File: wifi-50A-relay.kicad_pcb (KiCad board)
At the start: 2 copper layers, 85 x 56 mm, 42 parts, among them J1 PROG, J2 100k_HOT, J3 100k_COLD, K1 J115F21C12VDCS.9, K2 J115F21C12VDCS.9, Q1 AO3400A, SW1 SKRKAEE020, U1 ESP-WROOM-02, U2 TPS54331DR, U3 ADS1115IDGS

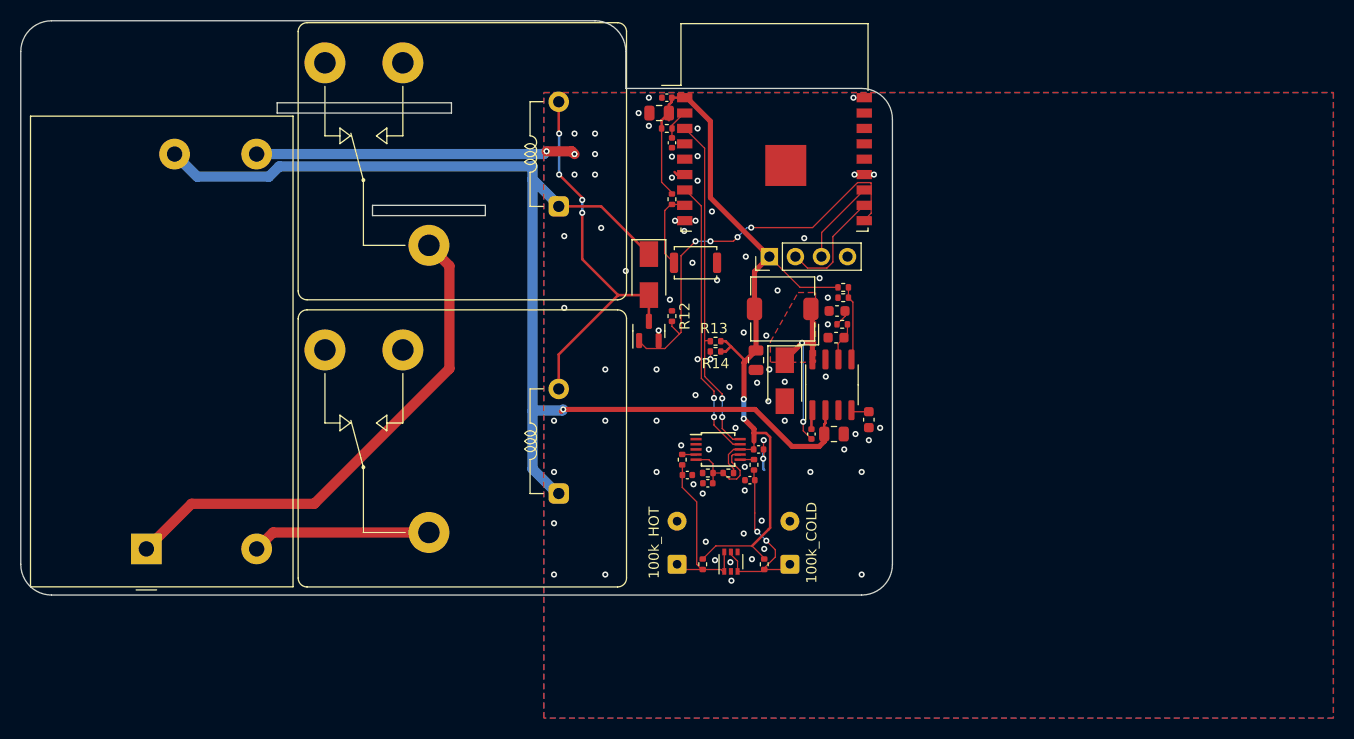
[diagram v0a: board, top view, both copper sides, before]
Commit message: Add kibot & fix DRC issues from kicad update
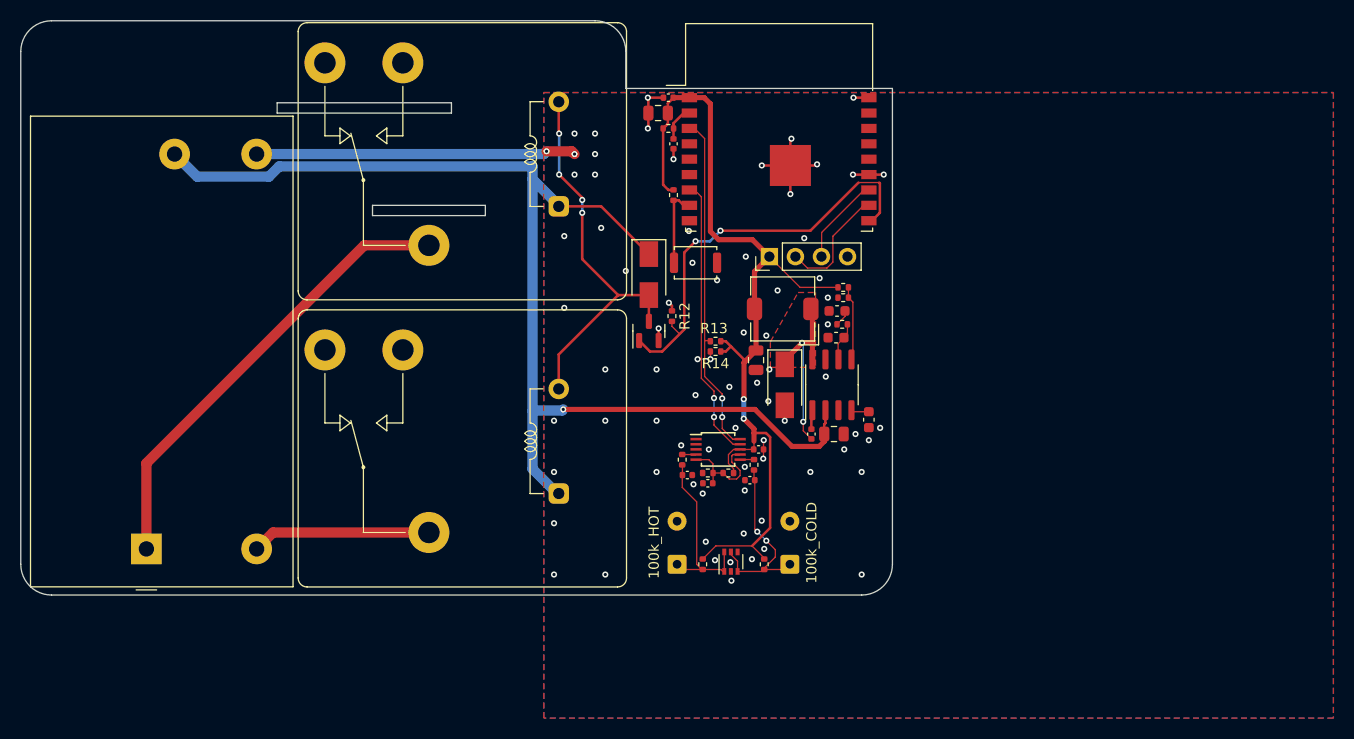
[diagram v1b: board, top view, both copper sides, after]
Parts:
- moved U1 0.45 mm to (102.0, 44.5)
- moved R3 0.43 mm to (91.7, 48.0)
- moved D1 0.40 mm to (102.5, 66.5)
- moved C8 0.18 mm to (91.7, 43.0)
- moved C5 0.15 mm to (91.2, 38.5)
- moved R2 0.15 mm to (91.2, 41.5)
- moved C3 0.10 mm to (90.2, 40.0)
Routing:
- net GND: track 36.0 -> 56.1 mm, vias 80 -> 75
- net /AC_PH_2: track 49.7 -> 44.7 mm
- net /SW: track 39.5 -> 42.9 mm, vias 4 -> 2
- net +3V3: track 88.2 -> 90.3 mm
- net Net-(C12-Pad1): track 18.4 -> 17.1 mm
- net Net-(C11-Pad1): track 17.5 -> 16.7 mm
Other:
- outline, holes or cut-outs redrawn

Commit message: Fix erc issues
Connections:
- net +3V3 renamed +3.3V
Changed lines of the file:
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@@
   (net 2 "+12V")
   (net 3 "Net-(C2-Pad1)")
-  (net 4 "+3V3")
+  (net 4 "+3.3V")
   (net 5 "Net-(C4-Pad1)")
   (net 6 "Net-(C6-Pad1)")
@@
     (fp_line (start 1 0.625) (end -1 0.625) (layer "F.Fab") (width 0.1))
     (pad "1" smd roundrect (at -0.95 0 180) (size 1 1.45) (layers "F.Cu" "F.Paste" "F.Mask") (roundrect_rratio 0.25)
-      (net 4 "+3V3") (pintype "passive"))
+      (net 4 "+3.3V") (pintype "passive"))
     (pad "2" smd roundrect (at 0.95 0 180) (size 1 1.45) (layers "F.Cu" "F.Paste" "F.Mask") (roundrect_rratio 0.25)
       (net 1 "GND") (pintype "passive"))
@@
     (fp_line (start -0.5 -0.25) (end 0.5 -0.25) (layer "F.Fab") (width 0.1))
     (pad "1" smd roundrect (at -0.48 0 180) (size 0.56 0.62) (layers "F.Cu" "F.Paste" "F.Mask") (roundrect_rratio 0.25)
-      (net 4 "+3V3") (pintype "passive"))
+      (net 4 "+3.3V") (pintype "passive"))
     (pad "2" smd roundrect (at 0.48 0 180) (size 0.56 0.62) (layers "F.Cu" "F.Paste" "F.Mask") (roundrect_rratio 0.25)
       (net 1 "GND") (pintype "passive"))
@@
     (fp_line (start -1 -0.625) (end 1 -0.625) (layer "F.Fab") (width 0.1))
     (pad "1" smd roundrect (at -0.95 0 270) (size 1 1.45) (layers "F.Cu" "F.Paste" "F.Mask") (roundrect_rratio 0.25)
-      (net 4 "+3V3") (pintype "passive"))
+      (net 4 "+3.3V") (pintype "passive"))
     (pad "2" smd roundrect (at 0.95 0 270) (size 1 1.45) (layers "F.Cu" "F.Paste" "F.Mask") (roundrect_rratio 0.25)
       (net 1 "GND") (pintype "passive"))
@@
     (fp_line (start -0.5 0.25) (end -0.5 -0.25) (layer "F.Fab") (width 0.1))
     (pad "1" smd roundrect (at -0.48 0) (size 0.56 0.62) (layers "F.Cu" "F.Paste" "F.Mask") (roundrect_rratio 0.25)
-      (net 4 "+3V3") (pintype "passive"))
+      (net 4 "+3.3V") (pintype "passive"))
     (pad "2" smd roundrect (at 0.48 0) (size 0.56 0.62) (layers "F.Cu" "F.Paste" "F.Mask") (roundrect_rratio 0.25)
       (net 1 "GND") (pintype "passive"))
@@
     (fp_line (start -1.27 8.89) (end -1.27 -0.635) (layer "F.Fab") (width 0.1))
     (pad "1" thru_hole rect (at 0 0 90) (size 1.7 1.7) (drill 1) (layers *.Cu *.Mask)
-      (net 4 "+3V3") (pinfunction "Pin_1") (pintype "passive"))
+      (net 4 "+3.3V") (pinfunction "Pin_1") (pintype "passive"))
     (pad "2" thru_hole oval (at 0 2.54 90) (size 1.7 1.7) (drill 1) (layers *.Cu *.Mask)
       (net 16 "Net-(J1-Pad2)") (pinfunction "Pin_2") (pintype "passive"))
@@
       (net 7 "Net-(C7-Pad2)") (pinfunction "1") (pintype "passive"))
     (pad "2" smd roundrect (at 2.75 0 180) (size 1.5 2.2) (layers "F.Cu" "F.Paste" "F.Mask") (roundrect_rratio 0.25)
-      (net 4 "+3V3") (pinfunction "2") (pintype "passive"))
+      (net 4 "+3.3V") (pinfunction "2") (pintype "passive"))
     (model "${KICAD6_3DMODEL_DIR}/Inductor_SMD.3dshapes/L_TDK_SLF6028.wrl"
       (offset (xyz 0 0 0))
@@
     (fp_line (start -0.525 0.27) (end -0.525 -0.27) (layer "F.Fab") (width 0.1))
     (pad "1" smd roundrect (at -0.51 0) (size 0.54 0.64) (layers "F.Cu" "F.Paste" "F.Mask") (roundrect_rratio 0.25)
-      (net 4 "+3V3") (pintype "passive"))
+      (net 4 "+3.3V") (pintype "passive"))
     (pad "2" smd roundrect (at 0.51 0) (size 0.54 0.64) (layers "F.Cu" "F.Paste" "F.Mask") (roundrect_rratio 0.25)
       (net 9 "/EN") (pintype "passive"))
@@
     (fp_line (start -0.525 0.27) (end -0.525 -0.27) (layer "F.Fab") (width 0.1))
     (pad "1" smd roundrect (at -0.51 0 270) (size 0.54 0.64) (layers "F.Cu" "F.Paste" "F.Mask") (roundrect_rratio 0.25)
-      (net 4 "+3V3") (pintype "passive"))
+      (net 4 "+3.3V") (pintype "passive"))
     (pad "2" smd roundrect (at 0.51 0 270) (size 0.54 0.64) (layers "F.Cu" "F.Paste" "F.Mask") (roundrect_rratio 0.25)
       (net 22 "/BOOT") (pintype "passive"))
@@
     (fp_line (start 0.525 -0.27) (end 0.525 0.27) (layer "F.Fab") (width 0.1))
     (pad "1" smd roundrect (at -0.51 0) (size 0.54 0.64) (layers "F.Cu" "F.Paste" "F.Mask") (roundrect_rratio 0.25)
-      (net 4 "+3V3") (pintype "passive"))
+      (net 4 "+3.3V") (pintype "passive"))
     (pad "2" smd roundrect (at 0.51 0) (size 0.54 0.64) (layers "F.Cu" "F.Paste" "F.Mask") (roundrect_rratio 0.25)
       (net 23 "Net-(R4-Pad2)") (pintype "passive"))
@@
     (fp_line (start 0.525 0.27) (end -0.525 0.27) (layer "F.Fab") (width 0.1))
     (pad "1" smd roundrect (at -0.51 0 270) (size 0.54 0.64) (layers "F.Cu" "F.Paste" "F.Mask") (roundrect_rratio 0.25)
-      (net 4 "+3V3") (pintype "passive"))
+      (net 4 "+3.3V") (pintype "passive"))
     (pad "2" smd roundrect (at 0.51 0 270) (size 0.54 0.64) (layers "F.Cu" "F.Paste" "F.Mask") (roundrect_rratio 0.25)
       (net 11 "Net-(C11-Pad1)") (pintype "passive"))
@@
     (fp_line (start 0.525 0.27) (end -0.525 0.27) (layer "F.Fab") (width 0.1))
     (pad "1" smd roundrect (at -0.51 0 270) (size 0.54 0.64) (layers "F.Cu" "F.Paste" "F.Mask") (roundrect_rratio 0.25)
-      (net 4 "+3V3") (pintype "passive"))
+      (net 4 "+3.3V") (pintype "passive"))
     (pad "2" smd roundrect (at 0.51 0 270) (size 0.54 0.64) (layers "F.Cu" "F.Paste" "F.Mask") (roundrect_rratio 0.25)
       (net 37 "Net-(C12-Pad1)") (pintype "passive"))
@@
     (fp_line (start 0.525 0.27) (end -0.525 0.27) (layer "F.Fab") (width 0.1))
     (pad "1" smd roundrect (at -0.51 0 180) (size 0.54 0.64) (layers "F.Cu" "F.Paste" "F.Mask") (roundrect_rratio 0.25)
-      (net 4 "+3V3") (pintype "passive"))
+      (net 4 "+3.3V") (pintype "passive"))
     (pad "2" smd roundrect (at 0.51 0 180) (size 0.54 0.64) (layers "F.Cu" "F.Paste" "F.Mask") (roundrect_rratio 0.25)
       (net 26 "/1.65V") (pintype "passive"))
@@
     (fp_line (start -8.5 -6) (end -9 -5.5) (layer "F.Fab") (width 0.1))
     (pad "1" smd rect (at -8.75 -6) (size 1.5 0.9) (layers "F.Cu" "F.Paste" "F.Mask")
-      (net 4 "+3V3") (pinfunction "VDD") (pintype "power_in"))
+      (net 4 "+3.3V") (pinfunction "VDD") (pintype "power_in"))
     (pad "2" smd rect (at -8.75 -4.5) (size 1.5 0.9) (layers "F.Cu" "F.Paste" "F.Mask")
       (net 9 "/EN") (pinfunction "EN") (pintype "input"))
@@
       (net 26 "/1.65V") (pinfunction "AIN3") (pintype "input"))
     (pad "8" smd rect (at 2.15 0) (size 1.1 0.25) (layers "F.Cu" "F.Paste" "F.Mask")
-      (net 4 "+3V3") (pinfunction "VDD") (pintype "power_in"))
+      (net 4 "+3.3V") (pinfunction "VDD") (pintype "power_in"))
     (pad "9" smd rect (at 2.15 -0.5) (size 1.1 0.25) (layers "F.Cu" "F.Paste" "F.Mask")
       (net 31 "/SDA") (pinfunction "SDA") (pintype "bidirectional"))
@@
     (fp_line (start 0.525 -0.27) (end 0.525 0.27) (layer "F.Fab") (width 0.1))
     (pad "1" smd roundrect (at -0.51 0 180) (size 0.54 0.64) (layers "F.Cu" "F.Paste" "F.Mask") (roundrect_rratio 0.25)
-      (net 4 "+3V3") (pintype "passive"))
+      (net 4 "+3.3V") (pintype "passive"))
     (pad "2" smd roundrect (at 0.51 0 180) (size 0.54 0.64) (layers "F.Cu" "F.Paste" "F.Mask") (roundrect_rratio 0.25)
       (net 27 "/SCL") (pintype "passive"))
@@
     (fp_line (start -0.525 -0.27) (end 0.525 -0.27) (layer "F.Fab") (width 0.1))
     (pad "1" smd roundrect (at -0.51 0 180) (size 0.54 0.64) (layers "F.Cu" "F.Paste" "F.Mask") (roundrect_rratio 0.25)
-      (net 4 "+3V3") (pintype "passive"))
+      (net 4 "+3.3V") (pintype "passive"))
     (pad "2" smd roundrect (at 0.51 0 180) (size 0.54 0.64) (layers "F.Cu" "F.Paste" "F.Mask") (roundrect_rratio 0.25)
       (net 31 "/SDA") (pintype "passive"))

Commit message: Replace hand-soldered connectors with JST-XH
These seem to be the most common connector for the 3950 100k NTC
connectors found in 3d printers.
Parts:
- 100k_COLD: renamed from J3; footprint Connector_Wire:SolderWire-0.25sqmm_1x02_P4.2mm_D0.65mm_OD1.7mm -> Connector_JST:JST_XH_B2B-XH-AM_1x02_P2.50mm_Vertical
- 100k_HOT: renamed from J2; footprint Connector_Wire:SolderWire-0.25sqmm_1x02_P4.2mm_D0.65mm_OD1.7mm -> Connector_JST:JST_XH_B2B-XH-AM_1x02_P2.50mm_Vertical
- moved 100k_COLD 3.09 mm to (105.7, 82.5)
- moved 100k_HOT 1.98 mm to (90.7, 82.5)
- moved D3 1.12 mm to (98.4, 83.8)
- moved R6 1.12 mm to (95.6, 84.0)
- moved R7 1.12 mm to (101.6, 84.0)
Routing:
- net Net-(C12-Pad1): track 17.1 -> 21.5 mm
- net Net-(C11-Pad1): track 16.7 -> 21.0 mm
- net GND: vias 75 -> 73
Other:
- board text added: "50A water heater controller flaviutamas.com/p/50a-wh-controller"
- board text added: "WARNING: - do not crimp solid-core wire - do not crimp fine-strand wire - use UL listed wire & connectors - use 10AWG wire or thicker - use 6in long wire or shorter - use correctly sized wire nuts"
